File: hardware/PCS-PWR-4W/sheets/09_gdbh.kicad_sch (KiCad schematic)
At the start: 131 parts, among them Q901 PMV30ENEAR, Q902 PMV30ENEAR, Q903 PMV30ENEAR, Q904 PMV30ENEAR, Q905 PMV30ENEAR, Q906 PMV30ENEAR, Q907 PMV30ENEAR, Q908 ZXTP25040DFHTA, Q909 ZXTP25040DFHTA, Q910 ZXTP25040DFHTA, Q911 ZXTN25040DFHTA, Q912 MMBT3904,215, Q913 MMBT3906,215, Q914 MMBT3904,215, U901 SN74LVC1G17DBVR, U902 NSI6651ASC-Q1SWR

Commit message: Respond to the independent re-check R2 of a427981 (D-078, D-079): gates-off commutation closed, backup band lowered, SiC acceptance, bounded grid-forming transients, ride-through without derating, AC-start repairs, installation requirements
- Register gen/data/review_r2.csv: 14 findings verified and dispositioned (9 Confirmed, 1 Firmware Handled,
  1 Improvement Recommended, 2 Already Fixed, 1 Not Applicable), every row closed with its evidence
- D-078 power stage: the discrete window turns the gates off at 520.8 A, not at the 485.5 A window top; the leg deck
  at that current peaked at 1457 V against 1445 V, closed at zero cost by R_G,off 7.5 -> 8.75 ohm (1437 V, admissible
  533.6 A); L1 inductance trajectory to 700 A (knee 566 A), CMPSS backup band lowered to 423.9-497.5 A on PCS-CTL,
  firmware OV backup 1035 V; R_DS(on) <= 40 mOhm acceptance with per-lot derating; one coil contract (20 W / 4 W);
  residual-current monitor contract; docs/requirements/INSTALLATION.md (74 enforceable requirements with sources)
- D-079 control study: tolerance regression at the assembly tolerances (1,944 + 1,000 cases, worst PM 48.1 deg);
  bounded grid-forming transients 0.43 / 1.77 pu with feed-forward and OV deadbeat (2.17 pu superseded), trip-aware
  DC-load rejection, CV-mode soft-OV hold, weak-grid CV power limits, PV DC-bus coordination row (0.51 ms);
  ride-through 270 A clamp with C_f prediction removes the stiff-grid derating (fallback kept, SCR estimator,
  8.07 MVA declaration); coupled four-wire cases; AC start in the executable state machine (17 states, 35 fault
  cases) with the five sequence holes H1-H5 repaired and an own AC_STOP state
- pcs_spec protection_chain published and read by the control study and the control board; all 15 boards, BOMs,
  costs, comparisons (PV 2/24/3/5/0, PCS 2/38/4/9/0), audits and figures regenerated; README, guide 03-13,
  decisions mirror and architecture reconciliation notes updated; .graphifyignore and graphify-out/ ignored

Co-Auth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
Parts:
- R909, R915, R921, R927, R933, R939: value 7.5R -> 8.75R
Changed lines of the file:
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@@
 			)
 		)
-		(property "Value" "7.5R"
+		(property "Value" "8.75R"
 			(at 408.94 68.456 90)
 			(show_name no)
@@
 			)
 		)
-		(property "Description" "Resistor 7.5R 1% 2512 Roff, pulse-rated thick film 1 W"
+		(property "Description" "Resistor 8.75R 1% 2512 Roff, pulse-rated thick film 1 W"
 			(at 408.94 66.04 0)
 			(hide yes)
@@
 			)
 		)
-		(property "Value" "7.5R"
+		(property "Value" "8.75R"
 			(at 185.42 93.856 90)
 			(show_name no)
@@
 			)
 		)
-		(property "Description" "Resistor 7.5R 1% 2512 Roff, pulse-rated thick film 1 W"
+		(property "Description" "Resistor 8.75R 1% 2512 Roff, pulse-rated thick film 1 W"
 			(at 185.42 91.44 0)
 			(hide yes)
@@
 			)
 		)
-		(property "Value" "7.5R"
+		(property "Value" "8.75R"
 			(at 309.88 119.256 90)
 			(show_name no)
@@
 			)
 		)
-		(property "Description" "Resistor 7.5R 1% 2512 Roff, pulse-rated thick film 1 W"
+		(property "Description" "Resistor 8.75R 1% 2512 Roff, pulse-rated thick film 1 W"
 			(at 309.88 116.84 0)
 			(hide yes)
@@
 			)
 		)
-		(property "Value" "7.5R"
+		(property "Value" "8.75R"
 			(at 246.38 106.556 90)
 			(show_name no)
@@
 			)
 		)
-		(property "Description" "Resistor 7.5R 1% 2512 Roff, pulse-rated thick film 1 W"
+		(property "Description" "Resistor 8.75R 1% 2512 Roff, pulse-rated thick film 1 W"
 			(at 246.38 104.14 0)
 			(hide yes)
@@
 			)
 		)
-		(property "Value" "7.5R"
+		(property "Value" "8.75R"
 			(at 154.94 157.356 90)
 			(show_name no)
@@
 			)
 		)
-		(property "Description" "Resistor 7.5R 1% 2512 Roff, pulse-rated thick film 1 W"
+		(property "Description" "Resistor 8.75R 1% 2512 Roff, pulse-rated thick film 1 W"
 			(at 154.94 154.94 0)
 			(hide yes)
@@
 			)
 		)
-		(property "Value" "7.5R"
+		(property "Value" "8.75R"
 			(at 373.38 131.956 90)
 			(show_name no)
@@
 			)
 		)
-		(property "Description" "Resistor 7.5R 1% 2512 Roff, pulse-rated thick film 1 W"
+		(property "Description" "Resistor 8.75R 1% 2512 Roff, pulse-rated thick film 1 W"
 			(at 373.38 129.54 0)
 			(hide yes)

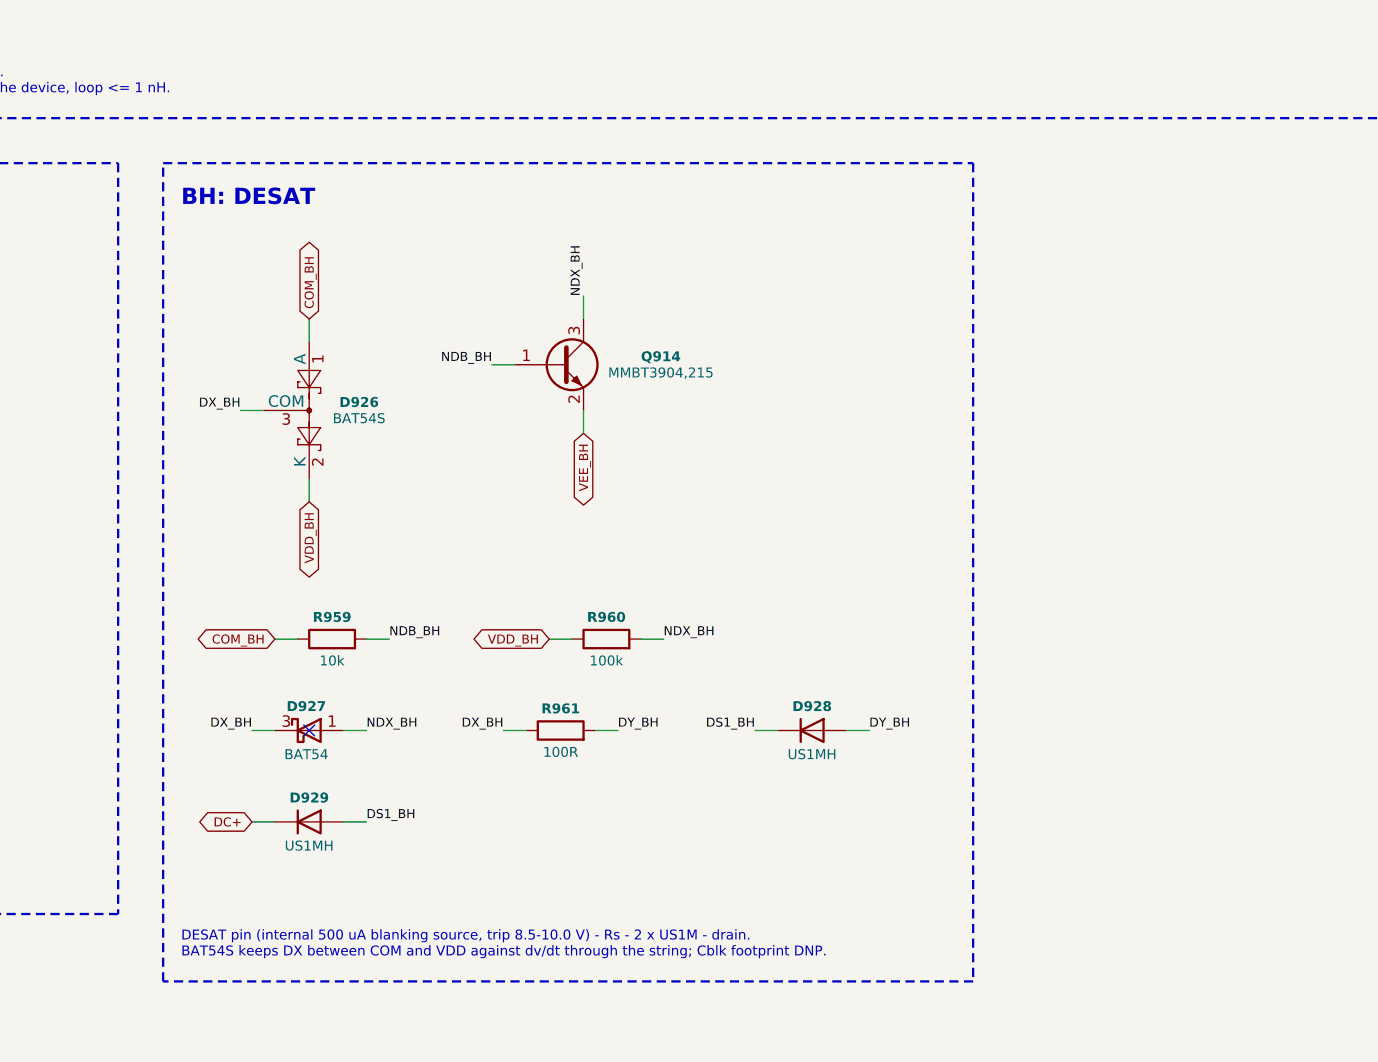
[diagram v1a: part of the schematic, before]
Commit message: Respond to the independent economical re-check R4 of 845131d (D-081): DESAT string re-rated to 1300 V diodes, cable-aware DC-bus window enforced, off-grid envelope stated as declared capability, inverter cold rating -10 C, grade-B rating stated, magnetics RFQ index
- Register gen/data/review_r4.csv: 12 decision areas closed (3 Confirmed, 4 Already Fixed, 3 Improvement Recommended, 2 Not Applicable)
- E01: the DESAT sense string sees the whole DC link (static envelope 1130 V) on an off switch; 2 x Vishay BYG23T-M3/TR (1300 V)
  per channel on both presets, each diode blocking the envelope alone; PCS window unchanged, PV preset 3 -> 2 diodes; grade
  tables identical; +0.96 to +2.12 USD per module at 5k; datasheet, prices, ledger rows, insulation table
- E04: inter-module cable in the coupled PCS/PV bus model (+28 V); product rule default set point 750 V (755 V four-wire mode A),
  782 V firmware clamp in the PV module, PCS refuses an island start above 791 V, 909 V recorded as model validity; harness contract
- E06: AC-04 reworded as the module's declared output capability with the release sequence (grid-following first)
- E11: PCS cold-start passive table modelled; rating full operation from -10 C inlet (AC-02 amended by delegation), cold fan RFQ open
- E05: grade-B rating 124.57 kW at PF 1 stated; E12: docs/requirements/RFQ-MAGNETICS.md (ten RFQs); the port CM ring's catalog
  entry set to the flat-permeability grade and the aux transformer's thermal test to the 94.2 W rating
- All 15 boards, BOMs, costs, comparisons (PV 2/24/3/5/0, PCS 2/38/4/9/0), audits (pin 192/0/55, insulation 98 known) and figures
  regenerated; README, guide 01-13, INSTALLATION.md (77 rows), decisions mirror and the registers updated

Co-Authored-By: Claude Fable 5.1 <noreply@anthropic.com>
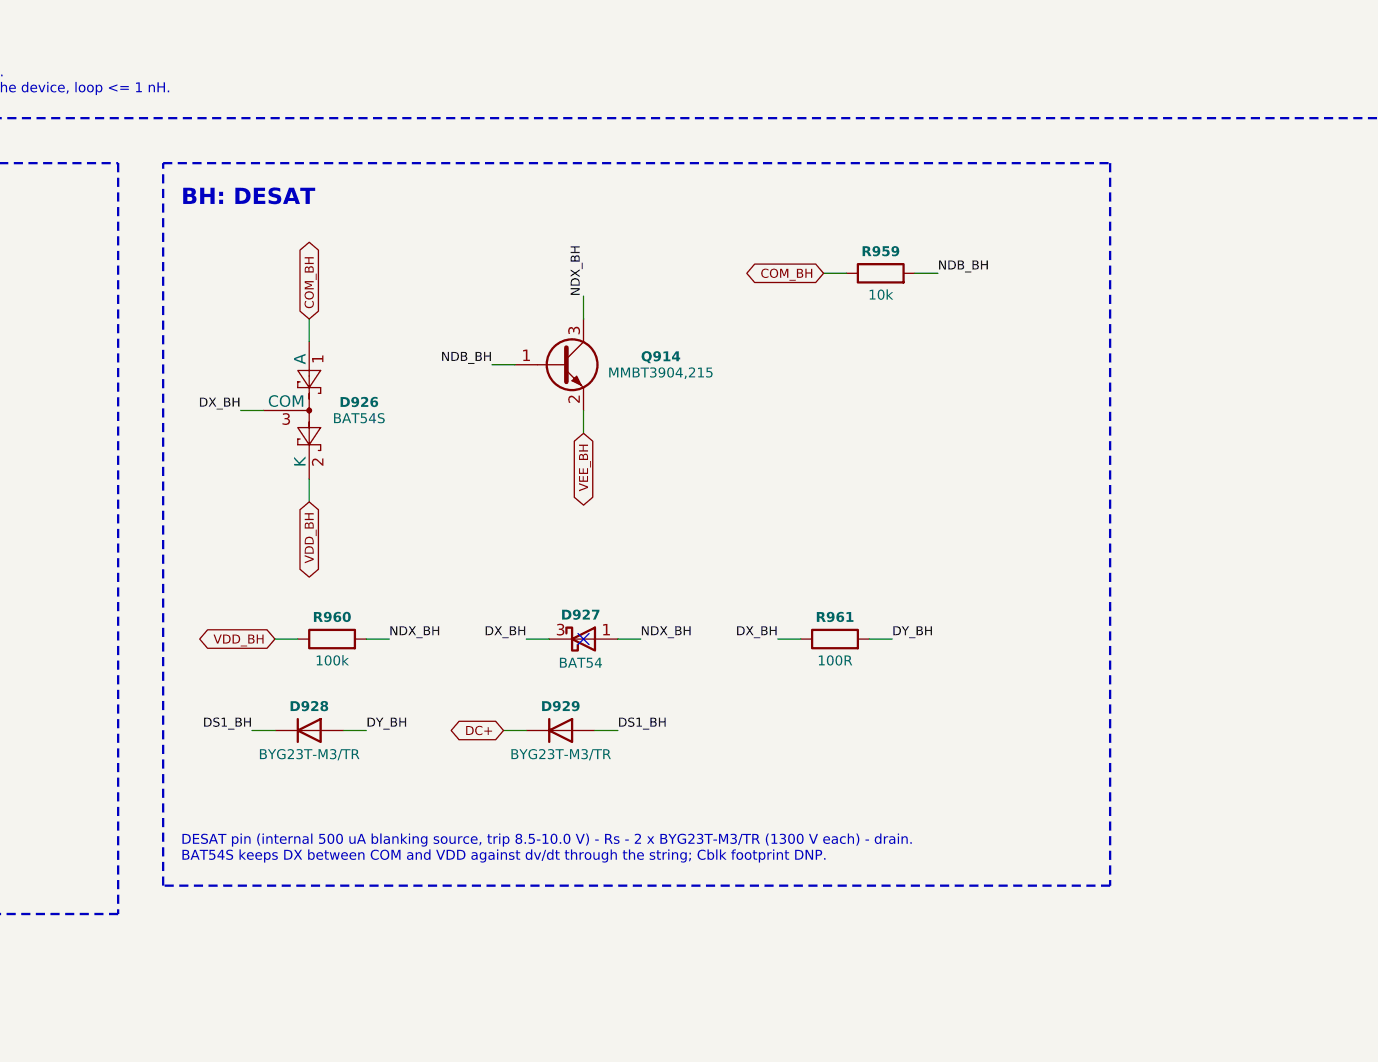
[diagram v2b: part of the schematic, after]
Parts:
- D928, D929: value US1MH -> BYG23T-M3/TR; symbol dcdc:US1M -> dcdc:BYG23T; MPN US1MH -> BYG23T-M3/TR; Manufacturer Taiwan Semiconductor -> Vishay
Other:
- note added: "DESAT pin (internal 500 uA blanking source, trip 8.5-10.0 V) - Rs - 2 x BYG23T-M3/TR (1300 V each) - drain. BAT54S keeps DX between COM and VDD against dv/dt through the string; Cblk footprint DNP."
- note removed: "DESAT pin (internal 500 uA blanking source, trip 8.5-10.0 V) - Rs - 2 x US1M - drain. BAT54S keeps DX between COM and VDD against dv/dt through the string; Cblk footprint DNP."
- moved on the sheet: D927, D928, D929, R959, R960, R961
